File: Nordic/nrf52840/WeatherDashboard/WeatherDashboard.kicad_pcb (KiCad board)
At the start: 4 copper layers, 103 x 80.1 mm, 51 parts, among them J1 Conn_01x02_Pin, J2 Conn_01x04_Pin, J3 524372471, J5 Conn_01x03_Pin, J6 2041119-1 (Mini Pcie Express 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, Q1 BSS138, Q2 AO3401A, Q3 SS8050, Q4 BSS84, Q5 BSS138, U1 MPM3805GQB-33-Z, U2 74LVC2G17GV_125

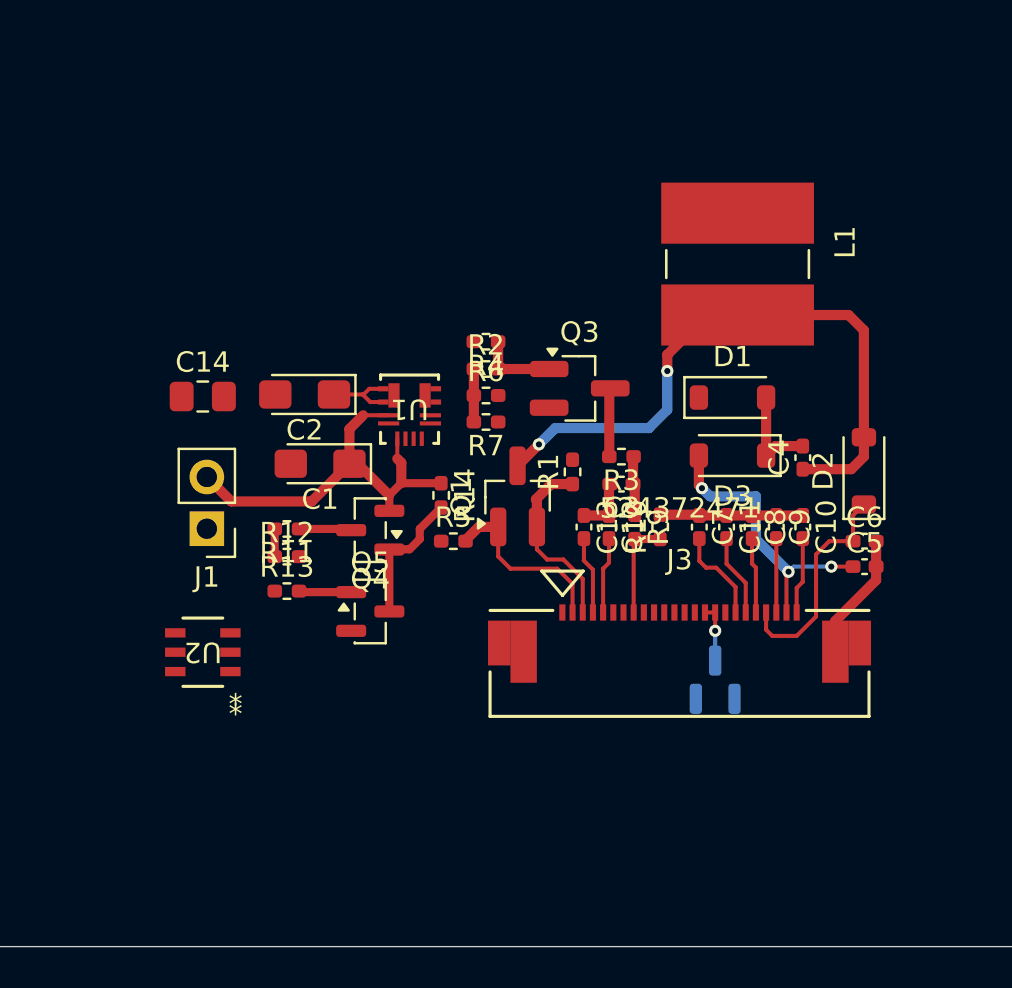
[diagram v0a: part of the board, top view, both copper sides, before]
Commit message: Update WeatherDashboard.kicad_pcb
updated hole for the display cable
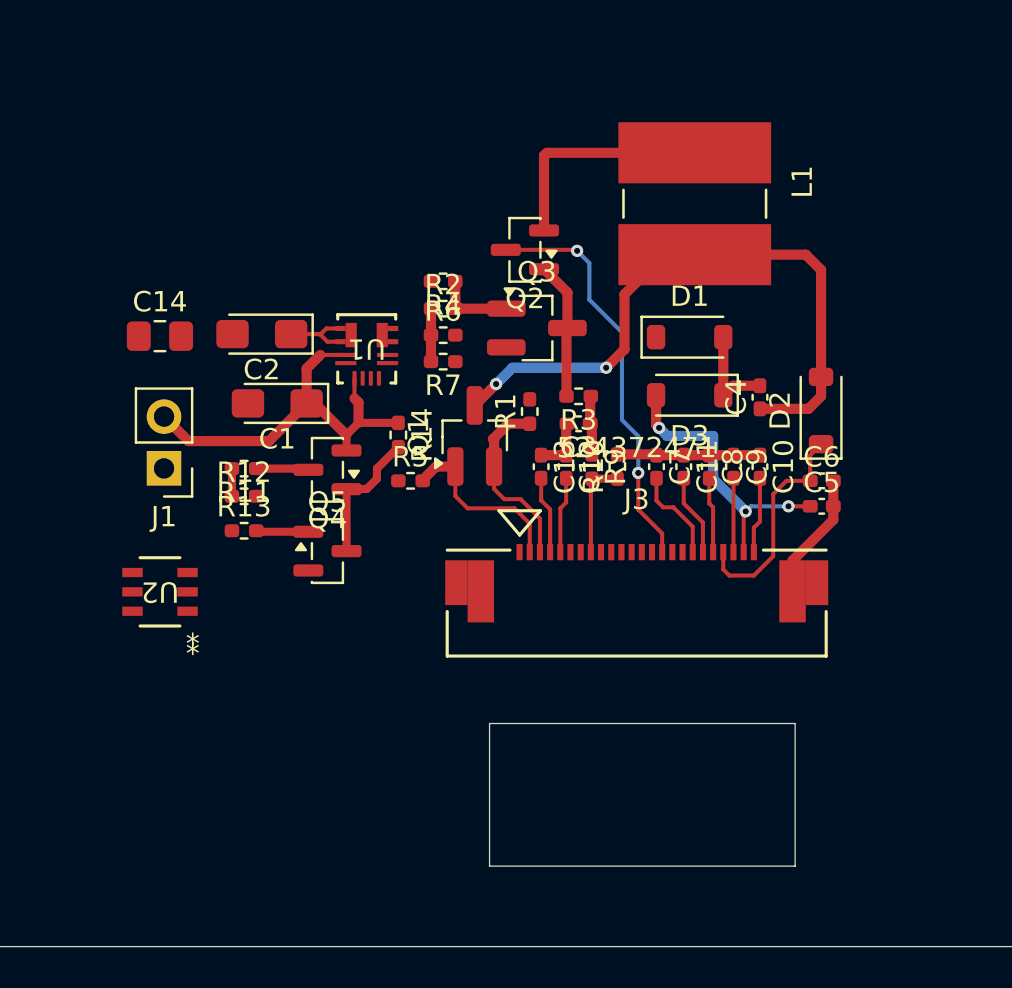
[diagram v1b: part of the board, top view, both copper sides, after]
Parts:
- Q2: moved to F.Cu
- moved Q2 23.1 mm to (160.1, 112.2), turned to 180 degrees
- moved C2 3.63 mm to (147.2, 116.4)
- moved C8 3.63 mm to (169.2, 122.9)
- moved C9 3.63 mm to (170.4, 122.9)
- moved J3 3.63 mm to (165.6, 129.6)
- moved R3 3.63 mm to (162.8, 119.4)
- moved U2 3.63 mm to (142.2, 129.0)
- moved C1 3.63 mm to (148.0, 119.8)
- moved C10 3.63 mm to (171.7, 122.9)
- moved C13 3.63 mm to (160.9, 122.9)
- moved C14 3.63 mm to (142.2, 116.5)
- moved C3 3.63 mm to (162.8, 120.8)
- moved C4 3.63 mm to (171.7, 119.5)
- moved C5 3.63 mm to (174.7, 124.8)
- moved C6 3.63 mm to (174.7, 123.6)
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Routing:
- net /Display/3v3_OUT: track 2.86 -> 20.0 mm, vias 1 -> 2
- net /Display/3v3: track 6.50 -> 17.6 mm
- net Net-(Q2-G): track 3.37 -> 6.73 mm
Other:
- outline, holes or cut-outs redrawn

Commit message: layout
update layout for the pcie connector
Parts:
- added R17: 10K, Resistor_SMD:R_0402_1005Metric_Pad0.72x0.64mm_HandSolder, F.Cu at (130.6, 122.2)
- added R18: 10K, Resistor_SMD:R_0402_1005Metric_Pad0.72x0.64mm_HandSolder, F.Cu at (129.0, 122.1)
- moved R8 48.5 mm to (131.0, 137.2), turned to 90 degrees
- moved J1 42.3 mm to (184.6, 126.4)
- moved R16 27.5 mm to (136.3, 119.0), turned to -90 degrees
- moved R15 26.4 mm to (140.4, 119.0), turned to -90 degrees
- moved C14 23.4 mm to (132.8, 137.9), turned to -90 degrees
- moved C15 18.7 mm to (137.7, 119.0), turned to 90 degrees
- moved C16 18.3 mm to (139.0, 119.0), turned to 90 degrees
- moved U2 8.64 mm to (136.3, 122.8)
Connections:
- J6 pad 11: unconnected-(J6-Pad11) -> /Display/EPD_DC
- J6 pad 13: unconnected-(J6-Pad13) -> /Display/~{EPD_CS}
- J6 pad 18: /Display/~{EPD_CS} -> unconnected-(J6-Pad18)
- J6 pad 20: /Display/EPD_DC -> unconnected-(J6-Pad20)
- J6 pad 22: /Display/EPD_BUSY -> unconnected-(J6-Pad22)
- J6 pad 24: /Display/~{EPD_RST} -> unconnected-(J6-Pad24)
- J6 pad 7: unconnected-(J6-Pad7) -> /Display/EPD_BUSY
- J6 pad 9: unconnected-(J6-Pad9) -> /Display/~{EPD_RST}
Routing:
- net Net-(C14-Pad1): track 0.00 -> 100.1 mm, vias 0 -> 4
- net Net-(U2-1A): track 0.00 -> 87.8 mm
- net Net-(U2-2A): track 0.00 -> 72.5 mm
- net /Display/EPD_SCK: track 0.00 -> 52.7 mm, vias 0 -> 2
- net /Display/EPD_DIN: track 0.00 -> 51.4 mm
- net GND: track 16.1 -> 66.1 mm, vias 0 -> 33
- net /Display/EPD_BUSY: track 0.00 -> 47.7 mm
- net /Display/~{EPD_RST}: track 0.00 -> 46.7 mm
- net /Display/TSDA: track 0.00 -> 45.7 mm, vias 0 -> 2
- net /Display/EPD_DC: track 0.00 -> 45.6 mm
- net /Display/~{EPD_CS}: track 0.00 -> 44.8 mm
- net /Display/TSCL: track 0.00 -> 41.4 mm, vias 0 -> 2
- net /Pcie Connector/AdcIn: track 1.36 -> 38.5 mm
- net /Display/3v3: track 17.6 -> 44.5 mm, vias 0 -> 17
- net /Power/VIN: track 20.6 -> 47.4 mm, vias 0 -> 2
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- added copper zone on In2.Cu, net /Display/3v3
- added copper zone on In1.Cu, net GND
